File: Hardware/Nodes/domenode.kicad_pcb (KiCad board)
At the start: 2 copper layers, 100 x 65 mm, 64 parts, among them J1 MIC_JUMPER, J10 3V3, J11 TOUCH, J12 5V, J13 CAN_BOARD, J14 CANV, J15 RGB_SHIELD, J16 RGB_SHIELD, J17 GROVE/I2C, J18 ISP, J19 CAN_IN, J2 MIC_HEADER, J20 CAN_OUT, J21 SWITCHES, J3 SW0, J6 POWER_TEST, J7 SPEAKER, J9 SENSOR, SW1 SW1, SW2 SW2, SW3 RESET, SW4 BOOT, U1 MINI-360, U2 AMS1117-3.3, U3 ESP32-WROOM, U5 TSDP341xx, U6 SN65HVD230

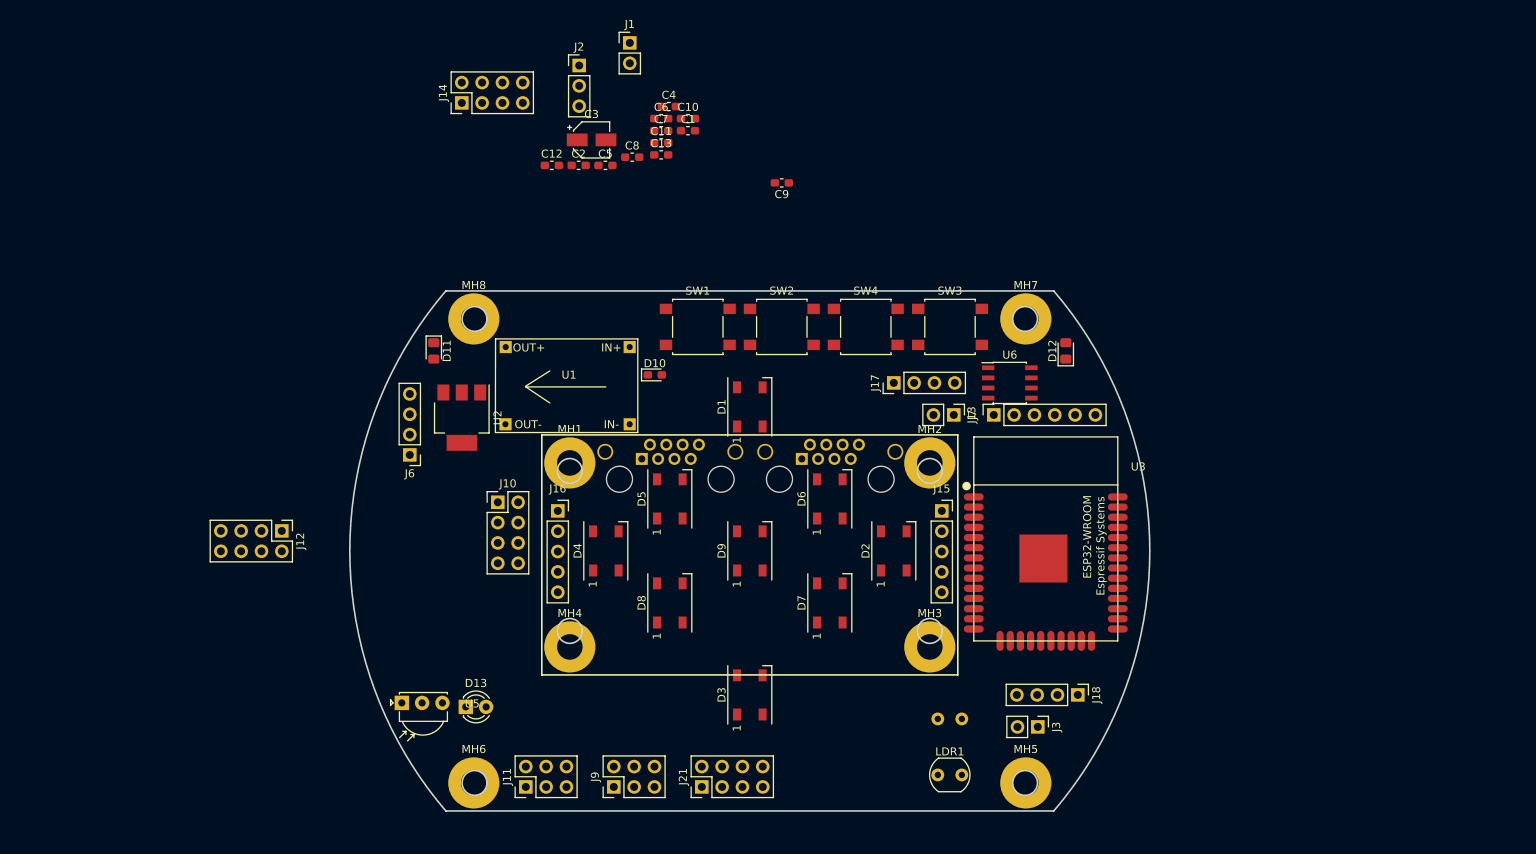
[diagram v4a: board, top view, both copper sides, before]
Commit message: Made board 5mm bigger, Moved ESP32 to back of board
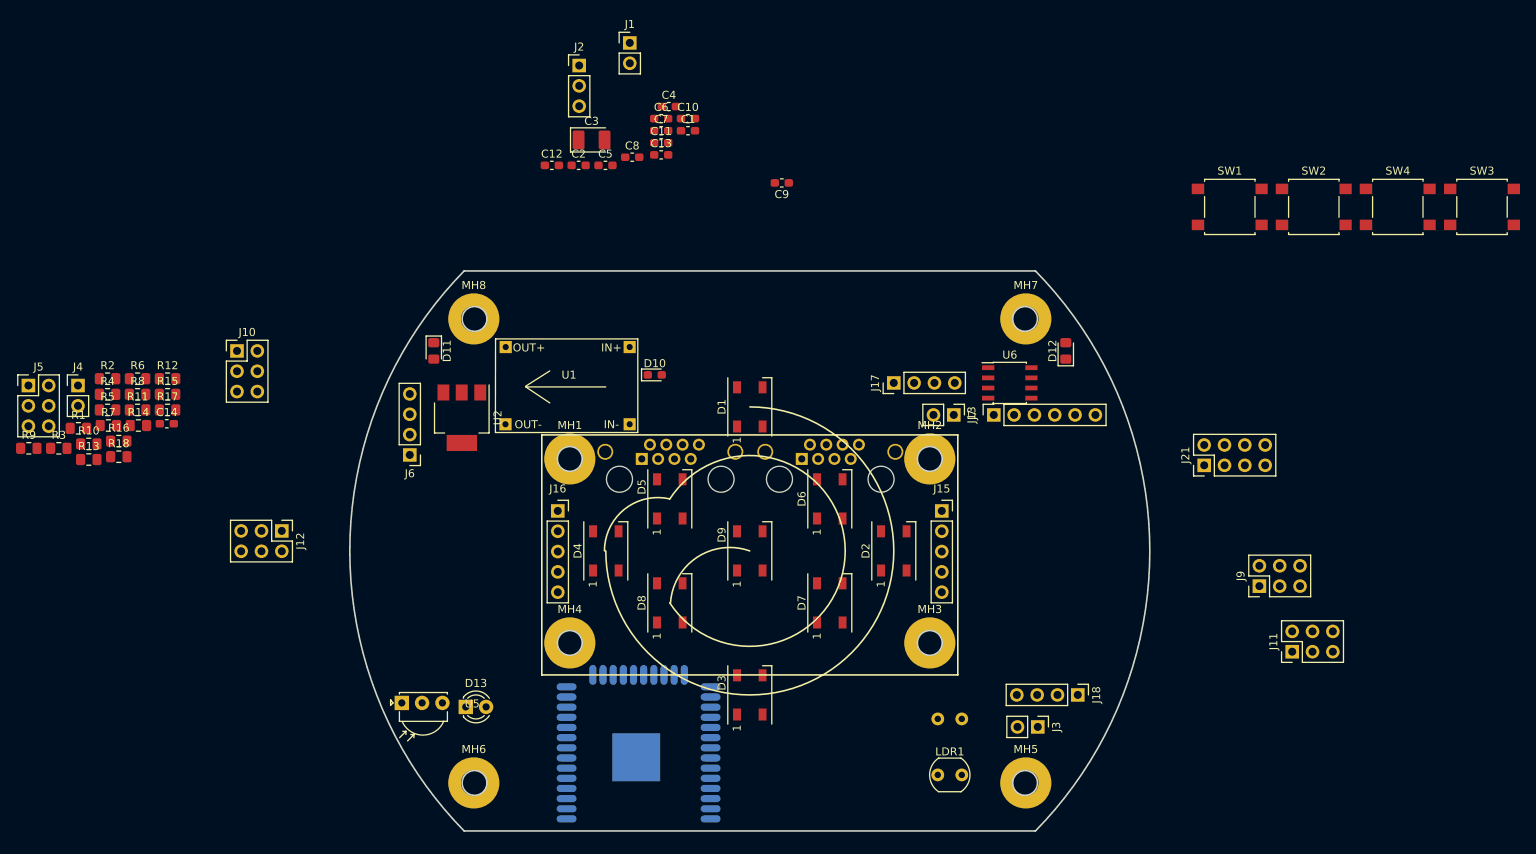
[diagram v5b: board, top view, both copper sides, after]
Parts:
- removed J14: CANV, Connector_PinHeader_2.54mm:PinHeader_2x04_P2.54mm_Vertical
- removed shm_logo_small: , shm_logo:shm_logo
- added C14: 100nF, Capacitor_SMD:C_0603_1608Metric_Pad1.05x0.95mm_HandSolder, F.Cu at (75.6, 89.1)
- added J4: CANTERM, Connector_PinHeader_2.54mm:PinHeader_1x02_P2.54mm_Vertical, F.Cu at (64.5, 84.3)
- added J5: 3V3, Connector_PinHeader_2.54mm:PinHeader_2x03_P2.54mm_Vertical, F.Cu at (58.3, 84.3)
- added R1: 100k, Resistor_SMD:R_0805_2012Metric_Pad1.15x1.40mm_HandSolder, F.Cu at (64.6, 89.7)
- added R10: 10k, Resistor_SMD:R_0805_2012Metric_Pad1.15x1.40mm_HandSolder, F.Cu at (65.9, 91.6)
- added R11: 100, Resistor_SMD:R_0805_2012Metric_Pad1.15x1.40mm_HandSolder, F.Cu at (72.0, 87.4)
- added R12: 1K, Resistor_SMD:R_0805_2012Metric_Pad1.15x1.40mm_HandSolder, F.Cu at (75.7, 83.5)
- added R13: 470, Resistor_SMD:R_0805_2012Metric_Pad1.15x1.40mm_HandSolder, F.Cu at (65.9, 93.6)
- added R14: 470, Resistor_SMD:R_0805_2012Metric_Pad1.15x1.40mm_HandSolder, F.Cu at (72.1, 89.3)
- added R15: 1K, Resistor_SMD:R_0805_2012Metric_Pad1.15x1.40mm_HandSolder, F.Cu at (75.7, 85.4)
- added R16: 100, Resistor_SMD:R_0805_2012Metric_Pad1.15x1.40mm_HandSolder, F.Cu at (69.6, 91.3)
- added R17: 10K, Resistor_SMD:R_0805_2012Metric_Pad1.15x1.40mm_HandSolder, F.Cu at (75.7, 87.4)
- added R18: 120, Resistor_SMD:R_0805_2012Metric_Pad1.15x1.40mm_HandSolder, F.Cu at (69.6, 93.2)
- added R2: 4K, Resistor_SMD:R_0805_2012Metric_Pad1.15x1.40mm_HandSolder, F.Cu at (68.2, 83.5)
- added R3: 5K, Resistor_SMD:R_0805_2012Metric_Pad1.15x1.40mm_HandSolder, F.Cu at (62.1, 92.2)
- added R4: 100k, Resistor_SMD:R_0805_2012Metric_Pad1.15x1.40mm_HandSolder, F.Cu at (68.2, 85.4)
- added R5: 10k, Resistor_SMD:R_0805_2012Metric_Pad1.15x1.40mm_HandSolder, F.Cu at (68.2, 87.4)
- added R6: 10k, Resistor_SMD:R_0805_2012Metric_Pad1.15x1.40mm_HandSolder, F.Cu at (72.0, 83.5)
- added R7: 10k, Resistor_SMD:R_0805_2012Metric_Pad1.15x1.40mm_HandSolder, F.Cu at (68.3, 89.3)
- added R8: 10k, Resistor_SMD:R_0805_2012Metric_Pad1.15x1.40mm_HandSolder, F.Cu at (72.0, 85.4)
- added R9: 10k, Resistor_SMD:R_0805_2012Metric_Pad1.15x1.40mm_HandSolder, F.Cu at (58.4, 92.2)
- C3: footprint Capacitor_SMD:CP_Elec_4x3.9 -> Capacitor_Tantalum_SMD:CP_EIA-3528-21_Kemet-B_Pad1.50x2.35mm_HandSolder
- J10: value 3V3 -> 5V; footprint Connector_PinHeader_2.54mm:PinHeader_2x04_P2.54mm_Vertical -> Connector_PinHeader_2.54mm:PinHeader_2x03_P2.54mm_Vertical
- J12: value 5V -> 24V; footprint Connector_PinHeader_2.54mm:PinHeader_2x04_P2.54mm_Vertical -> Connector_PinHeader_2.54mm:PinHeader_2x03_P2.54mm_Vertical
- SW1, SW2, SW3, SW4: footprint Buttons_Switches_SMD:SW_SPST_B3S-1000 -> Button_Switch_SMD:SW_SPST_B3S-1000
- U3: moved to B.Cu
- moved J11 97.3 mm to (216.3, 117.6)
- moved J9 84.5 mm to (212.2, 109.4)
- moved J21 74.6 mm to (205.3, 94.3)
- moved SW1 68.2 mm to (208.5, 62.0)
- moved SW2 68.2 mm to (219.0, 62.0)
- moved SW3 68.2 mm to (240.0, 62.0)
- moved SW4 68.2 mm to (229.5, 62.0)
- moved U3 59.0 mm to (134.6, 133.2)
- moved J10 37.7 mm to (84.4, 80.0)
- moved MH1 0.50 mm to (126.0, 93.5)
- moved MH2 0.50 mm to (171.0, 93.5)
- moved MH3 0.50 mm to (171.0, 116.5)
- moved MH4 0.50 mm to (126.0, 116.5)
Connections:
- net IO2 renamed Net-(U3-Pad24)
- C2 pad 1: REG5V -> +5V
- C4 pad 1: REG5V -> +5V
- C5 pad 1: REG3V3 -> VCC
- C7 pad 2: Net-(C7-Pad2) -> CANGND
- C9 pad 2: Net-(C9-Pad2) -> CANGND
- D6 pad 2: CANGND -> Net-(D6-Pad2)
- D7 pad 2: Net-(C9-Pad2) -> Net-(D7-Pad2)
- D7 pad 4: CANGND -> Net-(D6-Pad2)
- D8 pad 2: Net-(C7-Pad2) -> Net-(D8-Pad2)
- D8 pad 4: Net-(C9-Pad2) -> Net-(D7-Pad2)
- D9 pad 4: Net-(C7-Pad2) -> Net-(D8-Pad2)
- J10 pad 1: VCC -> +5V
- J10 pad 3: VCC -> +5V
- J10 pad 5: VCC -> +5V
- J12 pad 1: +5V -> +24V
- J12 pad 3: +5V -> +24V
- J12 pad 5: +5V -> +24V
- U1 pad 4: REG5V -> +5V
- U2 pad 2: REG3V3 -> VCC
- U2 pad 3: REG5V -> +5V
- U3 pad 12: Net-(U3-Pad12) -> RLDR
- U3 pad 14: RLDR -> Net-(U3-Pad14)
- U3 pad 15: Net-(U3-Pad15) -> CANGND
- U3 pad 18: Net-(U3-Pad18) -> IR_TX
- U3 pad 33: Net-(U3-Pad33) -> SW2
- U3 pad 36: Net-(U3-Pad36) -> BLINK
- U3 pad 37: Net-(U3-Pad37) -> SW1
- U3 pad 8: SW1 -> Net-(U3-Pad8)
- U3 pad 9: SW2 -> Net-(U3-Pad9)
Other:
- board size 100 x 65 mm -> 100 x 70 mm

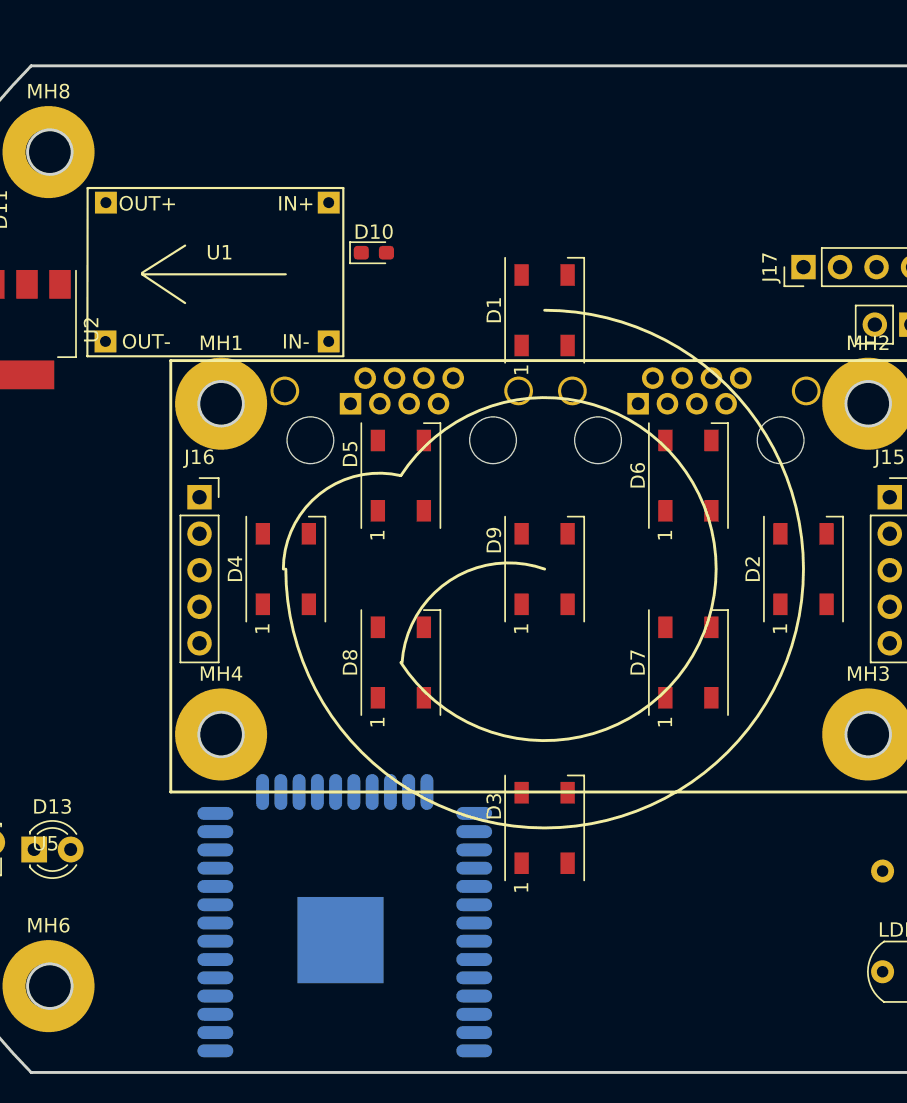
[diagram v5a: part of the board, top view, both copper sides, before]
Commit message: Added generic RJ45 connector footprint.
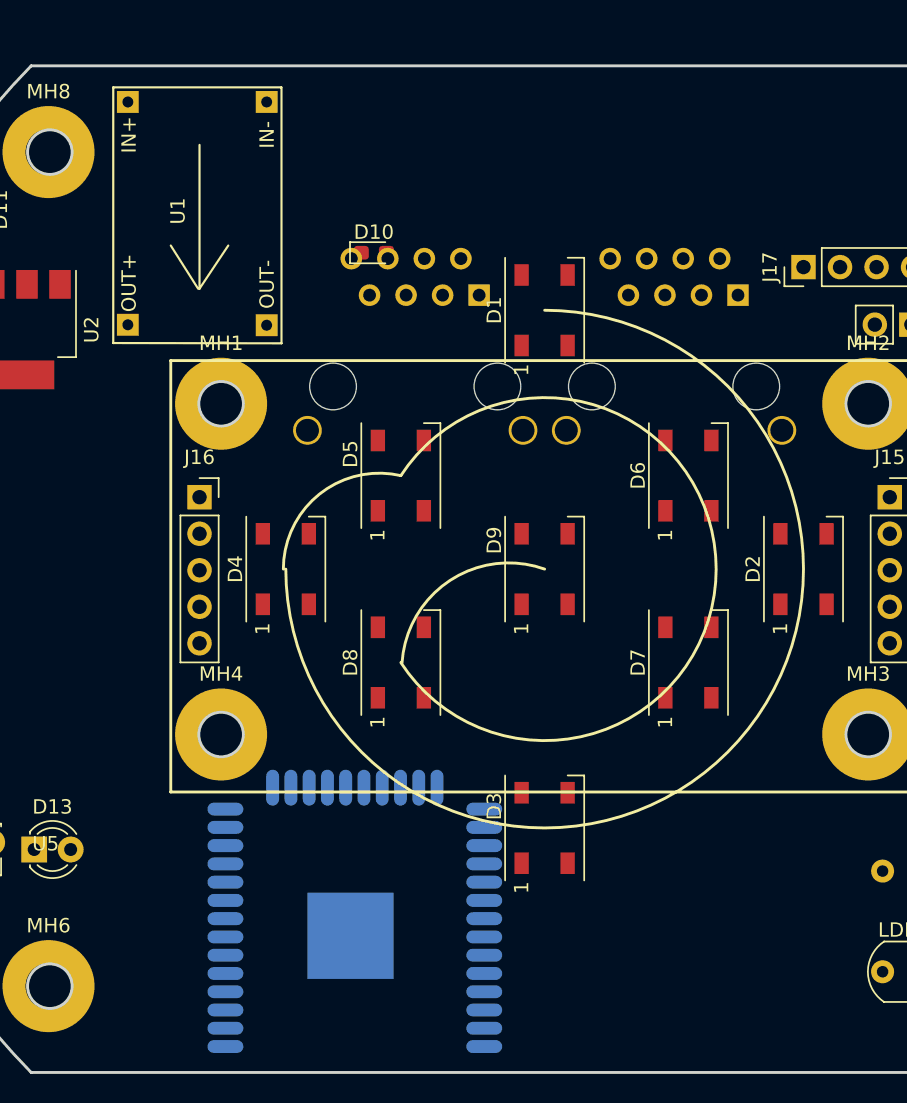
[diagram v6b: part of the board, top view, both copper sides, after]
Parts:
- J19, J20: footprint Connector_RJ:RJ45_Amphenol_RJHSE5380 -> RJ45:RJ45_GENERIC
- moved U1 17.5 mm to (118.5, 71.5), turned to 270 degrees
- moved J20 4.66 mm to (139.5, 92.3), turned to 180 degrees
- moved J19 2.77 mm to (157.5, 92.3), turned to 180 degrees
- moved U3 0.76 mm to (135.3, 132.9)

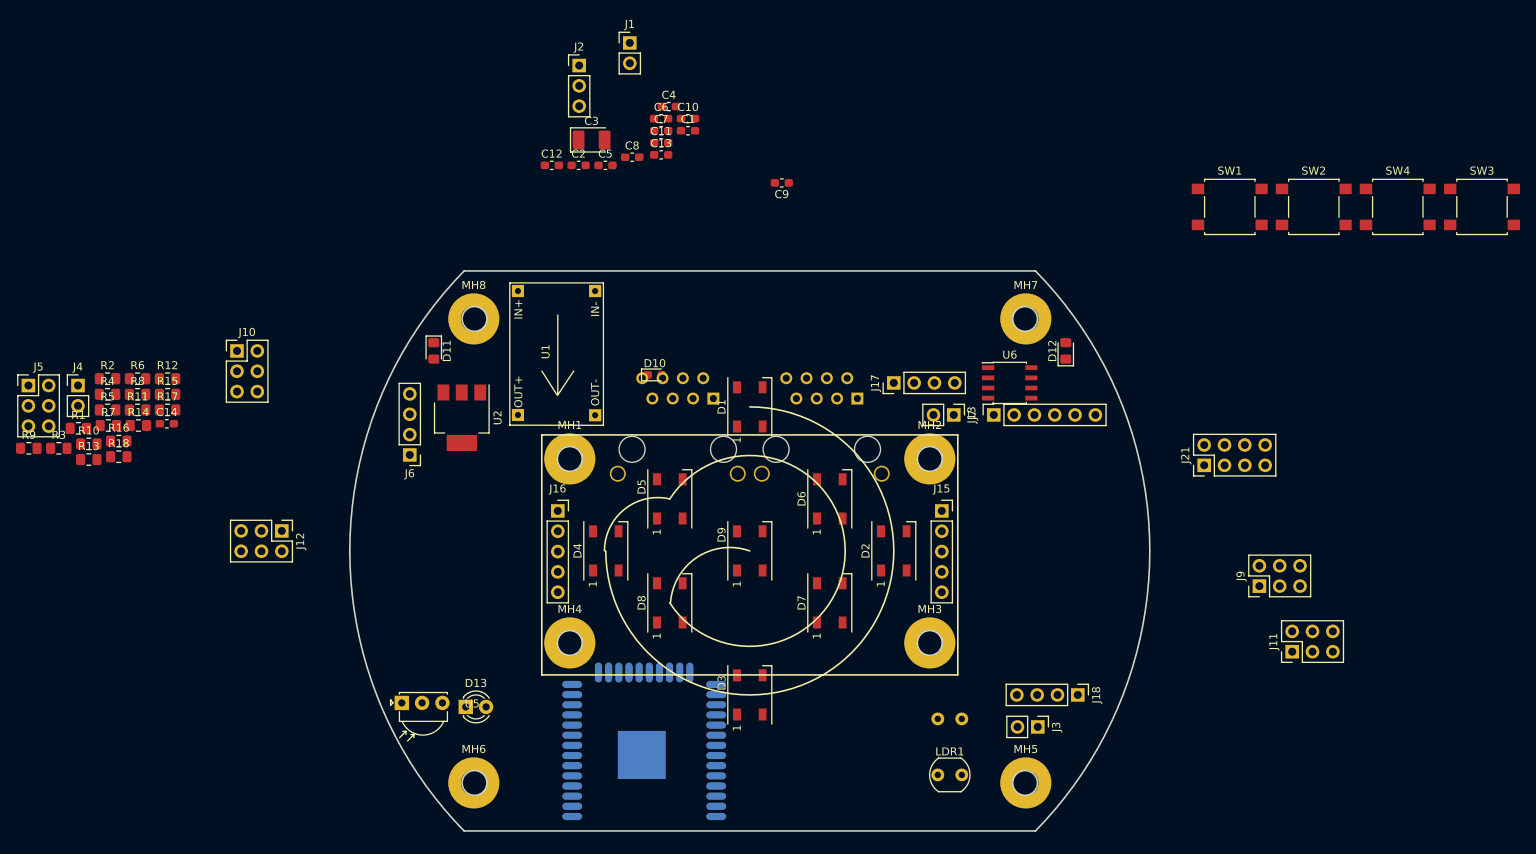
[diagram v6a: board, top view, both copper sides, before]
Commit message: Added 3D RJ45 model
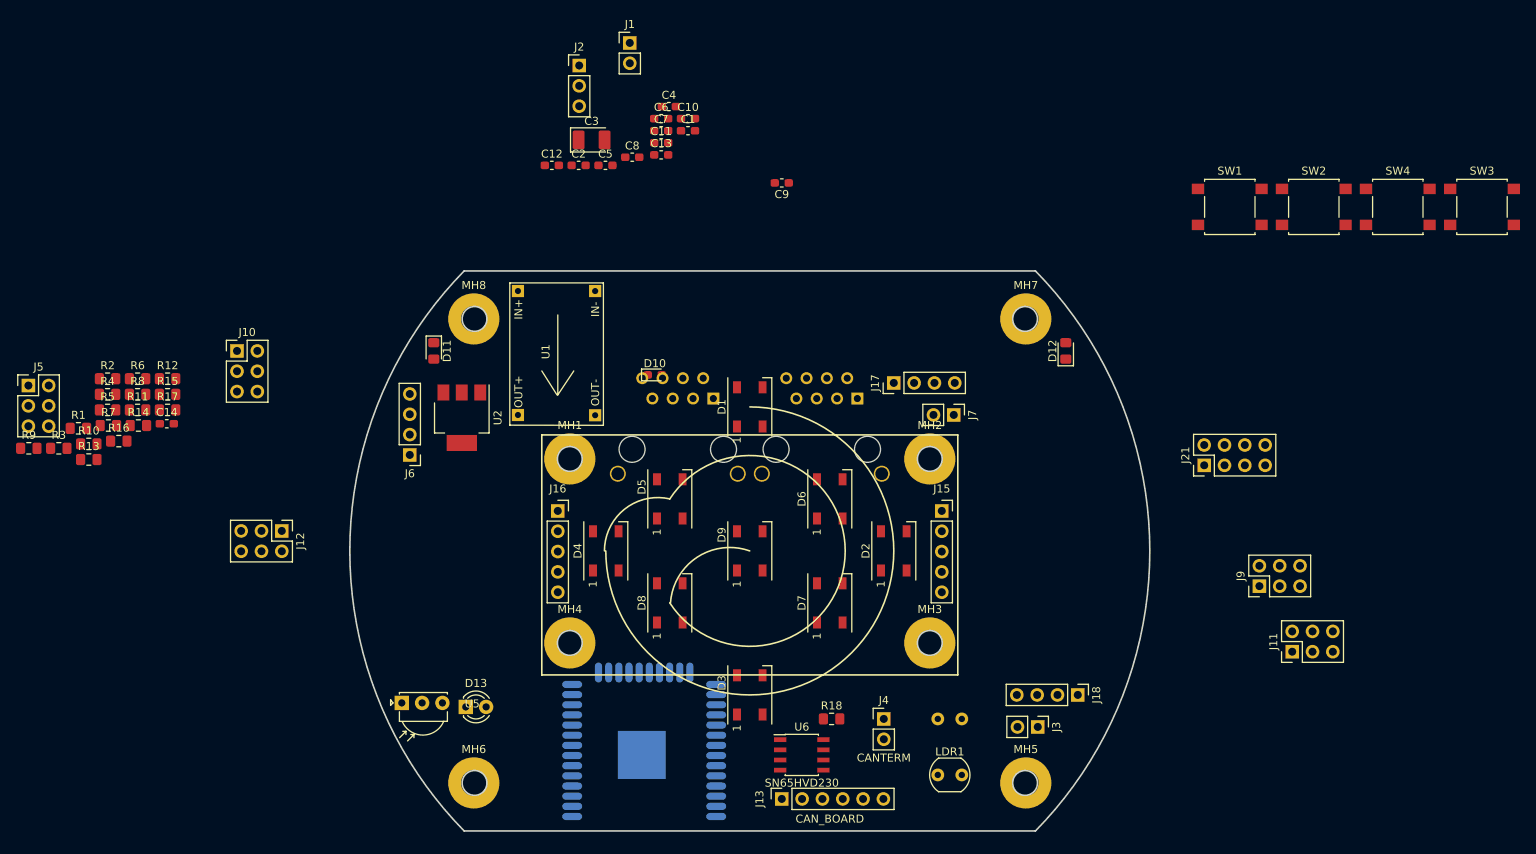
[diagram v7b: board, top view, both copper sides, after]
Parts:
- moved J4 109.0 mm to (165.2, 126.0)
- moved R18 94.9 mm to (158.7, 126.0)
- moved J13 54.8 mm to (152.5, 136.0)
- moved U6 53.3 mm to (155.0, 130.5)
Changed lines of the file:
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@@
       (rotate (xyz 0 0 0))
+    )
+    (model "${KIPRJMOD}/kicad_libraries/3dmodels/wurth_615008143721 (rev1).stp"
+      (offset (xyz 0 -2 6))
+      (scale (xyz 1 1 1))
+      (rotate (xyz 0 0 -90))
     )
   )
@@
       (scale (xyz 1 1 1))
       (rotate (xyz 0 0 0))
+    )
+    (model "${KIPRJMOD}/kicad_libraries/3dmodels/wurth_615008143721 (rev1).stp"
+      (offset (xyz 0 -2 6))
+      (scale (xyz 1 1 1))
+      (rotate (xyz 0 0 -90))
     )
   )
@@
   )
   (module Package_SO:SOIC-8_3.9x4.9mm_P1.27mm (layer F.Cu)
-    (at 181 84)
+    (at 155 130.5)
     (descr "8-Lead Plastic Small Outline (SN) - Narrow, 3.90 mm Body [SOIC] (see Microchip Packaging Specification 00000049BS.pdf)")
     (tags "SOIC 1.27")
@@
       (effects (font (size 1 1) (thickness 0.15)))
     )
-    (fp_text value SN65HVD230 (at 0 3.5) (layer F.Fab)
+    (fp_text value SN65HVD230 (at 0 3.5) (layer F.SilkS)
       (effects (font (size 1 1) (thickness 0.15)))
     )
@@
   )
   (module Connector_PinSocket_2.54mm:PinSocket_1x06_P2.54mm_Vertical (layer F.Cu)
-    (at 179 88 90)
+    (at 152.5 136 90)
     (descr "Through hole straight socket strip, 1x06, 2.54mm pitch, single row (from Kicad 4.0.7), script generated")
     (tags "Through hole socket strip THT 1x06 2.54mm single row")
@@
       (effects (font (size 1 1) (thickness 0.15)))
     )
-    (fp_text value CAN_BOARD (at 0 15.47 90) (layer F.Fab)
+    (fp_text value CAN_BOARD (at -2.5 6 180) (layer F.SilkS)
       (effects (font (size 1 1) (thickness 0.15)))
     )
@@
   )
   (module Connector_PinHeader_2.54mm:PinHeader_1x02_P2.54mm_Vertical (layer F.Cu)
-    (at 64.525001 84.325001)
+    (at 165.25 126)
     (descr "Through hole straight pin header, 1x02, 2.54mm pitch, single row")
     (tags "Through hole pin header THT 1x02 2.54mm single row")
@@
       (effects (font (size 1 1) (thickness 0.15)))
     )
-    (fp_text value CANTERM (at 0 4.87) (layer F.Fab)
+    (fp_text value CANTERM (at 0 4.87) (layer F.SilkS)
       (effects (font (size 1 1) (thickness 0.15)))
     )
@@
   )
   (module Resistor_SMD:R_0805_2012Metric_Pad1.15x1.40mm_HandSolder (layer F.Cu)
-    (at 69.625001 93.225001)
+    (at 158.725 126)
     (descr "Resistor SMD 0805 (2012 Metric), square (rectangular) end terminal, IPC_7351 nominal with elongated pad for handsoldering. (Body size source: https://docs.google.com/spreadsheets/d/1BsfQQcO9C6DZCsRaXUlFlo91Tg2WpOkGARC1WS5S8t0/edit?usp=sharing), generated with kicad-footprint-generator")
     (tags "resistor handsolder")
